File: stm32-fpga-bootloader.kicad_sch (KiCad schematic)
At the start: 88 parts, among them J1 USB_C_Receptacle_USB2.0_14P, J2 Conn_01x02, J3 RPI-TO-CPLD, J4 USB FPGA, J5 PMOD, J6 Conn_01x02, J7 TO-LCD, J8 CPLD-TO-RPI, J9 CPLD-TO-RPI, SW1 BOOT, SW2 RUN, SW3 ICE_BTN, SW4 ICE_RST, U1 RP2040, U2 W25Q128JVS, U3 LMV321, U4 ACPL-798J-500E, Y1 12Mhz

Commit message: Update the source files
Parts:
- removed C1, C4: 4.7u, Capacitor_SMD:C_0603_1608Metric, symbol Device:C_Small
- removed C10, C9: 10pF, Capacitor_SMD:C_0402_1005Metric, symbol Device:C_Small
- removed C2, C3, C5, C6, C7, C8: 100n, Capacitor_SMD:C_0402_1005Metric, symbol Device:C_Small
- removed D4: RED, LED_SMD:LED_0603_1608Metric, symbol Device:LED_Small
- removed J1: USB_C_Receptacle_USB2.0_14P, Connector_USB:USB_C_Receptacle_G-Switch_GT-USB-7010ASV, symbol Connector:USB_C_Receptacle_USB2.0_14P
- removed J4: USB FPGA, Connector_PinHeader_2.54mm:PinHeader_1x03_P2.54mm_Vertical, symbol Connector_Generic:Conn_01x03
- removed J7: TO-LCD, KiCadLocal:CON_536470274_MOL, symbol Connector_Generic:Conn_02x11_Odd_Even
- removed J8, J9: CPLD-TO-RPI, Connector_PinHeader_2.54mm:PinHeader_2x06_P2.54mm_Vertical, symbol Connector_Generic:Conn_02x06_Top_Bottom
- removed R1: 240R, Resistor_SMD:R_0402_1005Metric, symbol Device:R_Small
- removed R12: 1.2K, Resistor_SMD:R_0402_1005Metric, symbol Device:R_Small
- removed R2: 10R, Resistor_SMD:R_0402_1005Metric, symbol Device:R_Small
- removed R3, R4: 27R, Resistor_SMD:R_0402_1005Metric, symbol Device:R_Small
- removed R5: 10k, Resistor_SMD:R_0402_1005Metric, symbol Device:R_Small
- removed R6: 1k, Resistor_SMD:R_0402_1005Metric, symbol Device:R_Small
- removed SW1: BOOT, Button_Switch_SMD:SW_SPST_TL3342, symbol Switch:SW_Push
- removed U1: RP2040, Package_DFN_QFN:QFN-56-1EP_7x7mm_P0.4mm_EP3.2x3.2mm, symbol MCU_RaspberryPi:RP2040
- removed U2: W25Q128JVS, Package_SO:SOIC-8_5.3x5.3mm_P1.27mm, symbol Memory_Flash:W25Q128JVS
- removed Y1: 12Mhz, Crystal:Crystal_SMD_3225-4Pin_3.2x2.5mm, symbol Device:Crystal_GND24_Small
- added J14: CPLD_JTAG, Connector_PinHeader_2.54mm:PinHeader_1x06_P2.54mm_Vertical, symbol Connector_Generic:Conn_01x05
- added J8: USB_C_Receptacle_USB2.0_14P, Connector_USB:USB_C_Receptacle_G-Switch_GT-USB-7010ASV, symbol Connector:USB_C_Receptacle_USB2.0_14P
- added R59, R60, R61, R62: 0R, Resistor_SMD:R_0603_1608Metric, symbol Device:R_Small
- R30, R31, R33, R34, R35, R36: footprint Resistor_SMD:R_0402_1005Metric -> Resistor_SMD:R_0603_1608Metric
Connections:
- net CPLDK_SCK: now also A2.14 (GPIO10), A2.24 (GPIO18)
- net CPLD_B0_PT10A: now also A2.1 (GPIO0)
- net CPLD_B1_PT10B: now also A2.2 (GPIO1)
- net CPLD_B2_PT9A: now also A2.4 (GPIO2)
- net CPLD_B3_PT9B: now also A2.5 (GPIO3)
- net CPLD_B4_PR9A: now also A2.6 (GPIO4)
- net CPLD_B5_PR9B: now also A2.7 (GPIO5)
- net CPLD_B6_PR9C: now also A2.9 (GPIO6)
- net CPLD_B7_PR9D: now also A2.10 (GPIO7)
- net CPLD_MISO: now also A2.21 (GPIO16)
- net CPLD_MOSI: now also A2.25 (GPIO19)
- net CPLD_SCL: now also A2.27 (GPIO21)
- net CPLD_SDA: now also A2.26 (GPIO20)
- net CPLD_SPI_CS: now also A2.22 (GPIO17)
- net CPLD_SPI_MCS: now also A2.29 (GPIO22)
- net D+: now also R20.1, R22.1, J8.A6 (D+), J8.B6 (D+)
- net D-: now also R21.1, J8.A7 (D-), J8.B7 (D-)
- net GND: now also J14.5 (Pin_5), J8.A1 (GND), J8.A12 (GND), J8.B1 (GND), J8.B12 (GND), J8.S1 (SHIELD)
- new net: J8.A4 (VBUS), J8.A9 (VBUS), J8.B4 (VBUS), J8.B9 (VBUS)
- new net PT10C/TDO: J14.1 (Pin_1), R60.2
- new net PT10D/TDI: J14.2 (Pin_2), R59.2
- new net PT11C/TCK: J14.3 (Pin_3), R61.2
- new net PT11D/TMS: J14.4 (Pin_4), R62.2
- new net jtag-prog/TCK: R61.1
- new net jtag-prog/TDI: R59.1
- new net jtag-prog/TDO: R60.1
- new net jtag-prog/TMS: R62.1
- no-connect marks 57 -> 36
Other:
- added sheet jtag-prog (jtag-prog.kicad_sch)
- sheet displays ports: added CLOCK, DIG_1, DIG_2, DIG_3, DIG_4, DIG_DP, IO, KEY, LED_SEG, RTSW_A, RTSW_B; removed none
- sheet lcmxo2-cpld-block ports: added PL10C, PL10D; removed none
- note removed: "12MhZ Oscillator"
- note removed: "Flash Memory"
- note removed: "GPIO16_SPI0_RX GPIO19_SPI0_TX GPIO18_SPI0_SCK GPIO17_SPI0_CSn"
- note removed: "RP2040 MCU"
- moved on the sheet: A2, JP1, JP3, JP5, R20, R21, R22

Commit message: Update the schematic
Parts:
- removed SW2: RUN, EasyEDA_Lib:SW-SMD_L3.9-W3.0-P4.45, symbol EasyEDA_Lib:TS-1088-AR02016
- removed SW3: ICE_BTN, EasyEDA_Lib:SW-SMD_L3.9-W3.0-P4.45, symbol EasyEDA_Lib:TS-1088-AR02016
- removed SW4: ICE_RST, EasyEDA_Lib:SW-SMD_L3.9-W3.0-P4.45, symbol EasyEDA_Lib:TS-1088-AR02016
- added C48: 100n, Capacitor_SMD:C_0402_1005Metric, symbol Device:C_Small
- added C49: 10uF, Capacitor_SMD:C_0603_1608Metric, symbol Device:C_Small
- added J1001: DATA, symbol Connector_Generic:Conn_01x04
- added J15: Conn_01x02, TerminalBlock_Phoenix:TerminalBlock_Phoenix_PT-1,5-2-3.5-H_1x02_P3.50mm_Horizontal, symbol Connector_Generic:Conn_01x02
- added R73, R74, R75, R76, R77: 1.2K, Resistor_SMD:R_0603_1608Metric, symbol Device:R_Small
- added R78, R79, R80, R81, R82, R83: 100R, Resistor_SMD:R_0603_1608Metric, symbol Device:R_Small
- added SW2: RUN, EasyEDA_Lib:SW-SMD_L3.9-W3.0-P4.45, symbol Switch:SW_Push
- added SW3: ICE_BTN, EasyEDA_Lib:SW-SMD_L3.9-W3.0-P4.45, symbol Switch:SW_Push
- added SW4: ICE_RST, EasyEDA_Lib:SW-SMD_L3.9-W3.0-P4.45, symbol Switch:SW_Push
- added U13: ACPL-798J-500E, EasyEDA_Lib:SO-16_L10.3-W7.5-P1.27-LS10.6-BL, symbol EasyEDA_Lib:ACPL-798J-500E
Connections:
- net +3.3V: now also C48.1, C49.1, U13.1 (VDD1), U13.14 (VDD2), U13.7 (VDD1)
- net CPLDK_SCK: no longer A2.14 (GPIO10)
- net CPLD_CLOCK: now also A2.14 (GPIO10)
- net GND: now also C48.2, C49.2, J15.2 (Pin_2), R75.1, R77.1, SW2.1, SW3.1, SW4.1, U13.16 (GND2), U13.4 (GND1), U13.8 (GND1), U13.9 (GND2)
- net ICE_BTN: now also SW3.2
- net ICE_nRST: now also SW4.2
- net at A1.30 (RUN), R9.2: now also SW2.2
- new net: J1001.1 (Pin_1), R80.1
- new net: J1001.2 (Pin_2), R81.1
- new net: J1001.3 (Pin_3), R82.1
- new net: J1001.4 (Pin_4), R83.1
- new net: R79.1, R83.2, U13.10 (MDAT-)
- new net: R79.2, R82.2, U13.11 (MDAT+)
- new net: R78.1, R81.2, U13.12 (MCLKIN−)
- new net: R78.2, R80.2, U13.13 (MCLKIN+)
- new net: R76.2, U13.2 (VIN+)
- new net: R77.2, U13.3 (VIN-)
- new net: R74.2, R75.2, R76.1
- new net: J15.1 (Pin_1), R73.1
- new net: R73.2, R74.1
- no-connect marks 36 -> 28
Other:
- moved on the sheet: C15, C16, J6, R23, R24, R25, R26, R27, R30, R31, R33, R34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

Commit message: Update the schematic
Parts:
- removed J2: Conn_01x02, TerminalBlock_Phoenix:TerminalBlock_Phoenix_PT-1,5-2-3.5-H_1x02_P3.50mm_Horizontal, symbol Connector_Generic:Conn_01x02
- added C50, C51: 10uF, Capacitor_SMD:C_0603_1608Metric, symbol Device:C_Small
- added D1003, D1004, D1005: B5817W, PCM_JLCPCB:D_SOD-123, symbol PCM_JLCPCB-Diodes:Schottky,B5817W
- added U1: AMS1117-3.3, Package_TO_SOT_SMD:SOT-223-3_TabPin2, symbol Regulator_Linear:AMS1117-3.3
- J1001: footprint (none) -> Connector_PinSocket_2.54mm:PinSocket_1x04_P2.54mm_Vertical
- J15: footprint TerminalBlock_Phoenix:TerminalBlock_Phoenix_PT-1,5-2-3.5-H_1x02_P3.50mm_Horizontal -> Connector_PinSocket_2.54mm:PinSocket_1x02_P2.54mm_Vertical
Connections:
- net GND: now also C50.2, C51.2, U1.1 (GND)
- net VBUS1: now reaches A1.40 (VBUS)
- net VBUS1: now also D1003.2
- net VBUS2: now reaches A2.40 (VBUS)
- net VBUS2: now also D1004.2
- new net: C51.1, D1003.1, D1004.1, D1005.1, U1.3 (VI)
- new net: C50.1, U1.2 (VO)
- new net VBUS3: D1005.2
- no-connect marks 28 -> 26

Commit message: Update the footprints
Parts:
- removed C11, C12: 100n, Capacitor_SMD:C_0402_1005Metric, symbol Device:C_Small
- removed J14: CPLD_JTAG, Connector_PinHeader_2.54mm:PinHeader_1x06_P2.54mm_Vertical, symbol Connector_Generic:Conn_01x05
- removed R13: 1R, Resistor_SMD:R_0402_1005Metric, symbol Device:R_Small
- removed R14, R15, R16, R17, R18: 1.2K, Resistor_SMD:R_0402_1005Metric, symbol Device:R_Small
- removed R32: PEC11S-9213K-S0015, EasyEDA_Lib:RES-ADJ-SMD_PEC11S-9213K-S0015, symbol EasyEDA_Lib:PEC11S-9213K-S0015
- removed U13, U4: ACPL-798J-500E, EasyEDA_Lib:SO-16_L10.3-W7.5-P1.27-LS10.6-BL, symbol EasyEDA_Lib:ACPL-798J-500E
- removed U3: LMV321, Package_TO_SOT_SMD:SOT-23-5, symbol Amplifier_Operational:LMV321
- added J1002: JTAG JUMP, Connector_PinSocket_2.54mm:PinSocket_2x05_P2.54mm_Vertical, symbol Connector_Generic:Conn_02x05_Odd_Even
- added J1003: JTAG-LOG, Connector_PinSocket_2.54mm:PinSocket_1x03_P2.54mm_Vertical, symbol Connector_Generic:Conn_01x03
- added J1004: Conn_01x08, Connector_PinHeader_2.54mm:PinHeader_1x08_P2.54mm_Vertical, symbol Connector_Generic:Conn_01x08
- added R32: PEC11S-9213K-S0015, EasyEDA_Lib:RES-ADJ-SMD_PEC11S-9213K-S0015, symbol KiCadLocal:PEC11S-9213K-S0015
- added U13, U4: ACPL-798J-500E, EasyEDA_Lib:SO-16_L10.3-W7.5-P1.27-LS10.6-BL, symbol KiCadLocal:ACPL-798J-500E
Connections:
- net LED2 is gone; now on net IOT_50b: R11.1
- net UART1_RX is gone; now on net IOT_43a: A1.12 (GPIO9)
- net UART1_TX is gone; now on net IOB_23b: A1.11 (GPIO8)
- net +3.3V: now also C50.1, U1.2 (VO), U13.1 (VDD1), U13.14 (VDD2), U13.7 (VDD1), U4.1 (VDD1), U4.14 (VDD2), U4.7 (VDD1)
- net ENCODER_A: now also R32.A
- net ENCODER_B: now also R32.B
- net ENCODER_BTN: now also R32.D
- net GND: now also J1002.10 (Pin_10), J1002.9 (Pin_9), J1003.1 (Pin_1), J1004.8 (Pin_8), R32.C, R32.E, U13.16 (GND2), U13.4 (GND1), U13.8 (GND1), U13.9 (GND2), U4.16 (GND2), U4.4 (GND1), U4.8 (GND1), U4.9 (GND2); no longer A1.33 (AGND)
- net IOB_13b: now also J1004.2 (Pin_2)
- net IOB_20a: now also J1004.4 (Pin_4)
- net IOB_22a: now also J1004.5 (Pin_5)
- net IOB_23b: now also J1004.6 (Pin_6)
- net IOT_37a: now also J1004.3 (Pin_3)
- net IOT_43a: now also J1004.7 (Pin_7)
- net IOT_50b: now also J1004.1 (Pin_1)
- net LED1: now also A1.34 (GPIO28_ADC2)
- net PT10C/TDO: now also J1002.1 (Pin_1); no longer R60.2
- net PT10D/TDI: now also J1002.3 (Pin_3); no longer R59.2
- net PT11C/TCK: now also J1002.5 (Pin_5); no longer R61.2
- net PT11D/TMS: now also J1002.7 (Pin_7); no longer R62.2
- net jtag-prog/DBG_RX: now also J1003.2 (Pin_2)
- net jtag-prog/DBG_TX: now also J1003.3 (Pin_3)
- net at R79.1, R83.2: now also U13.10 (MDAT-)
- net at R79.2, R82.2: now also U13.11 (MDAT+)
- net at R78.1, R81.2: now also U13.12 (MCLKIN−)
- net at R78.2, R80.2: now also U13.13 (MCLKIN+)
- net at R76.2: now also U13.2 (VIN+)
- net at R77.2: now also U13.3 (VIN-)
- net at R31.2, R35.2: now also U4.11 (MDAT+)
- net +5V: now reaches C51.1, D1003.1, D1004.1, D1005.1, U1.3 (VI)
- net at R30.1, R34.2: now also U4.12 (MCLKIN−)
- net at R30.2, R33.2: now also U4.13 (MCLKIN+)
- net at R31.1, R36.2: now also U4.10 (MDAT-)
- net at R26.2: now also U4.2 (VIN+)
- net at R27.2: now also U4.3 (VIN-)
- new net TCK: J1002.6 (Pin_6), R61.2
- new net TDI: J1002.2 (Pin_2), R59.2
- new net TDO: J1002.4 (Pin_4), R60.2
- new net TMS: J1002.8 (Pin_8), R62.2
- no-connect marks 26 -> 36
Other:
- moved on the sheet: A2, C50, C51, D1003, D1004, D1005, D3, J5, J8, R11, R19, R20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

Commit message: Update the BOM and the routing
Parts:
- removed R59, R60, R61, R62: 0R, Resistor_SMD:R_0603_1608Metric, symbol Device:R_Small
- A1, A2, J1001, J1002, J1003, J1004, J15, J3, J5, J6: now not fitted; now left out of the parts list
- C13, C14, C17: LCSC (none) -> C1524
- C15, C48: LCSC (none) -> C1525
- C16, C49, C50, C51: LCSC (none) -> C19702
- D1, D2, D3: LCSC (none) -> C2286
- D1003, D1004, D1005: Attrition Qty 10 -> (none); Average Rectified Current (Io) 1A -> (none); Category Diodes,Schottky Barrier Diodes (SBD) -> (none); Class Preferred Component -> (none); Diode Configuration Single -> (none); Forward Voltage (Vf@If) 0.45V@1.0A -> (none); Minimum Qty 20 -> (none); Part B5817W -> (none); Peak forward surge current 9A -> (none); Price 0.019USD -> (none); Process SMT -> (none); Reverse Leakage Current (Ir) 1mA@20V -> (none); Reverse Voltage (Vr) 20V -> (none); Stock 146945 -> (none)
- JP1, JP2, JP3, JP4, JP5, JP6: now not fitted
- R10: LCSC (none) -> C25077
- R11, R7, R8: footprint Resistor_SMD:R_0402_1005Metric -> Resistor_SMD:R_0603_1608Metric; LCSC (none) -> C22765
- R19, R28, R29, R37, R9: LCSC (none) -> C11616
- R20: LCSC (none) -> C25867
- R21, R22: footprint Resistor_SMD:R_0402_1005Metric -> Resistor_SMD:R_0603_1608Metric; LCSC (none) -> C25190
- R23, R24, R25, R26, R27, R73, R74, R75, R76, R77: LCSC (none) -> C22765
- R30, R31, R33, R34, R35, R36, R78, R79, R80, R81, R82, R83: LCSC (none) -> C22775
- R32: Manufacturer Part PEC11S-9213K-S0015 -> (none); Supplier LCSC -> (none); Supplier Part C9900019227 -> (none); now not fitted; now left out of the parts list
- SW2, SW3, SW4: LCSC (none) -> C720477
- U1: LCSC (none) -> C6186
- U13, U4: Manufacturer Part ACPL-798J-500E -> (none); Supplier Part C961428 -> (none); now not fitted; now left out of the parts list
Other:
- sheet jtag-prog ports: added CLK; removed none
- sheet lcmxo2-cpld-block ports: added PL5B/PCLKC3_1; removed none
- moved on the sheet: C15, C16, C48, C49, R23, R24, R25, R26, R27, R30, R31, R33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

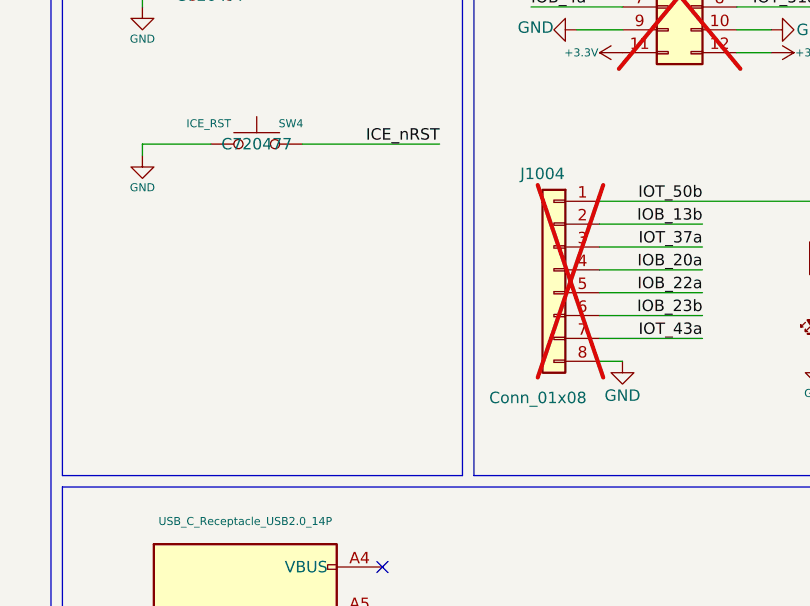
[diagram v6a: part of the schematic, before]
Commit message: Update the BOM and the routing
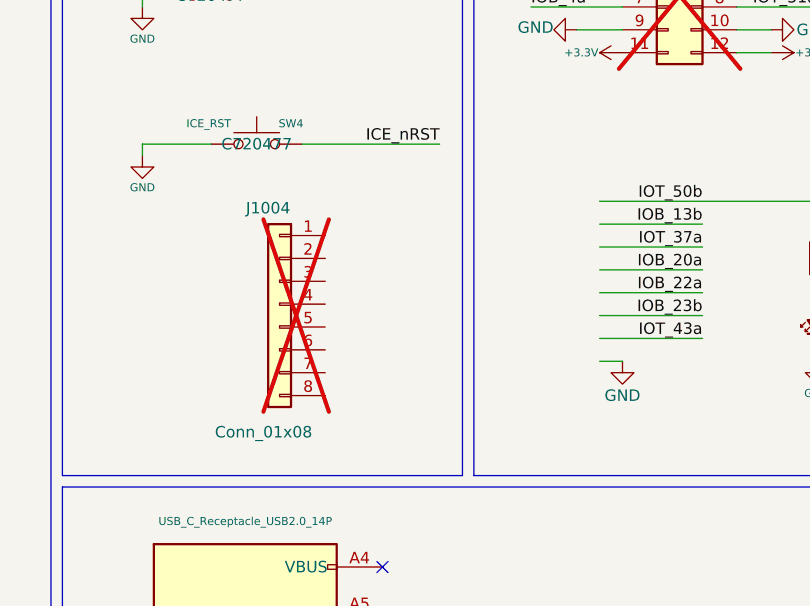
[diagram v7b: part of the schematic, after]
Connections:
- net GND: no longer J1004.8 (Pin_8)
- net IOB_13b: no longer J1004.2 (Pin_2)
- net IOB_20a: no longer J1004.4 (Pin_4)
- net IOB_22a: no longer J1004.5 (Pin_5)
- net IOB_23b: no longer J1004.6 (Pin_6)
- net IOT_37a: no longer J1004.3 (Pin_3)
- net IOT_43a: no longer J1004.7 (Pin_7)
- net IOT_50b: no longer J1004.1 (Pin_1)
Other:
- moved on the sheet: J1004
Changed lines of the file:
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@@
 	(symbol
 		(lib_id "Connector_Generic:Conn_01x08")
-		(at 191.77 59.69 0)
+		(at 161.29 63.5 0)
 		(mirror y)
 		(unit 1)
@@
 		(dnp yes)
 		(property "Reference" "J1004"
-			(at 190.5 49.022 0)
+			(at 160.02 52.832 0)
 			(effects
 				(font
@@
 		)
 		(property "Value" "Conn_01x08"
-			(at 189.992 73.914 0)
+			(at 159.512 77.724 0)
 			(effects
 				(font
@@
 		)
 		(property "Footprint" "Connector_PinHeader_2.54mm:PinHeader_1x08_P2.54mm_Vertical"
-			(at 191.77 59.69 0)
+			(at 161.29 63.5 0)
 			(effects
 				(font
@@
 		)
 		(property "Datasheet" "~"
-			(at 191.77 59.69 0)
+			(at 161.29 63.5 0)
 			(effects
 				(font
@@
 		)
 		(property "Description" "Generic connector, single row, 01x08, script generated (kicad-library-utils/schlib/autogen/connector/)"
-			(at 191.77 59.69 0)
+			(at 161.29 63.5 0)
 			(effects
 				(font
@@
 		)
 		(property "LCSC" "~"
-			(at 191.77 59.69 0)
+			(at 161.29 63.5 0)
 			(effects
 				(font
